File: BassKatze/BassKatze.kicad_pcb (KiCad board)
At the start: 2 copper layers, 55 x 54.9 mm, 50 parts, among them J1 Conn_01x02_Female, Q1 IRF7404, Q2 BSS138, SW1 SW_Push, U1 ATmega328-AU, U2 MSGEQ7, U3 TP4056

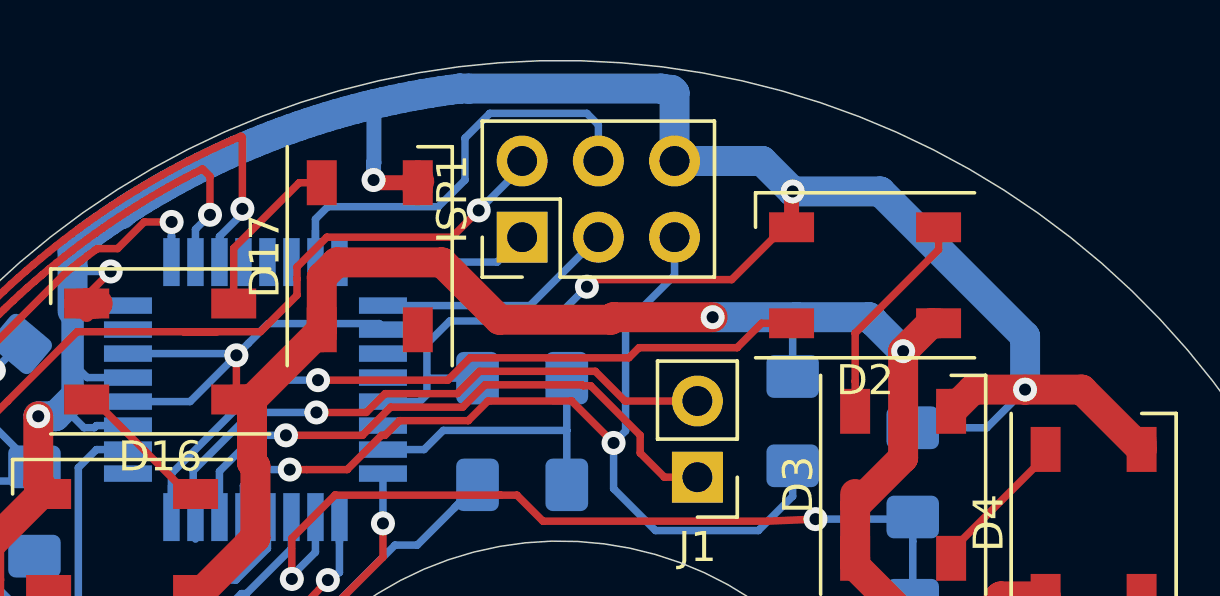
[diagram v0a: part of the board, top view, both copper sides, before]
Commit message: add pretective resistor to data pin of arduino
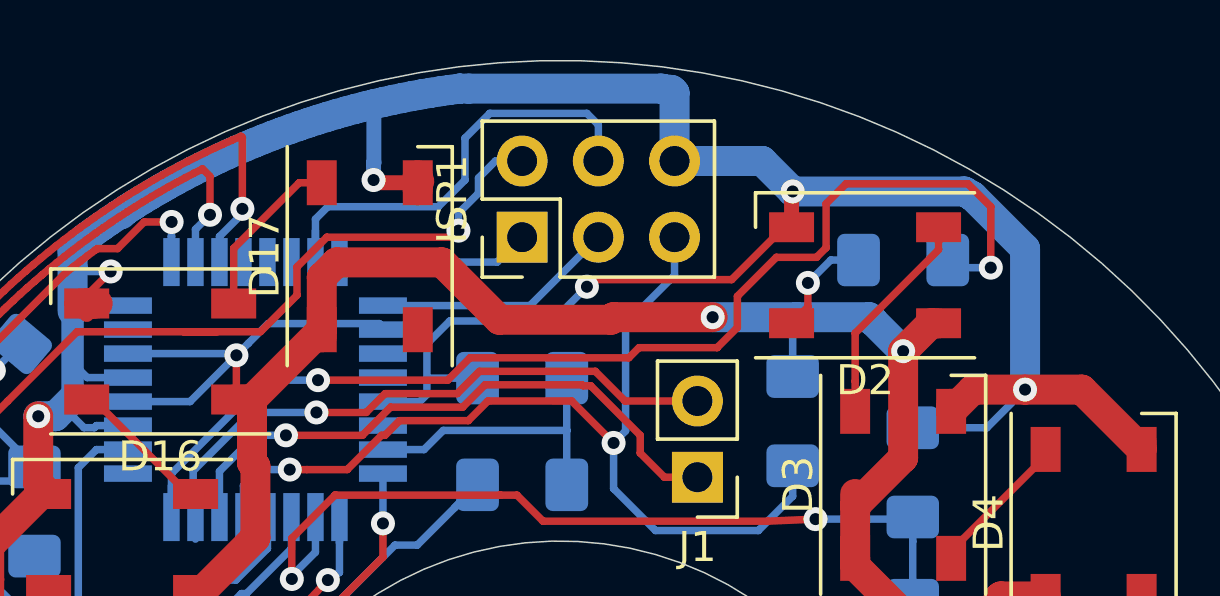
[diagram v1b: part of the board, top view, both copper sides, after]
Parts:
- added R14: 470Ohm, Resistor_SMD:R_1206_3216Metric_Pad1.42x1.75mm_HandSolder, B.Cu at (138.4, 106.2)
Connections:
- U1 pad 32: LED1 -> Net-(R14-Pad2)
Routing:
- net Net-(R14-Pad2): track 0.00 -> 39.2 mm, vias 0 -> 2
- net LED1: track 25.2 -> 3.57 mm
- net BAT-: track 283.6 -> 285.3 mm
- net 5V_Flash: track 27.5 -> 28.2 mm
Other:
- board text added: "BassKatze Rev 0.4"
- board text removed: "BassKatze Rev 0.3"

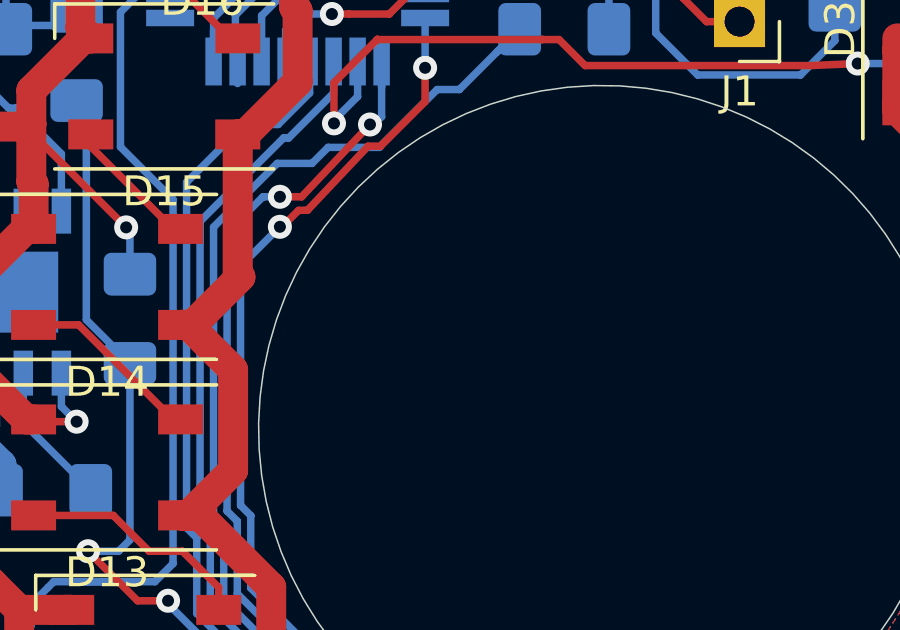
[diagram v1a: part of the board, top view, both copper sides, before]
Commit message: Added R16, added modes to sketch
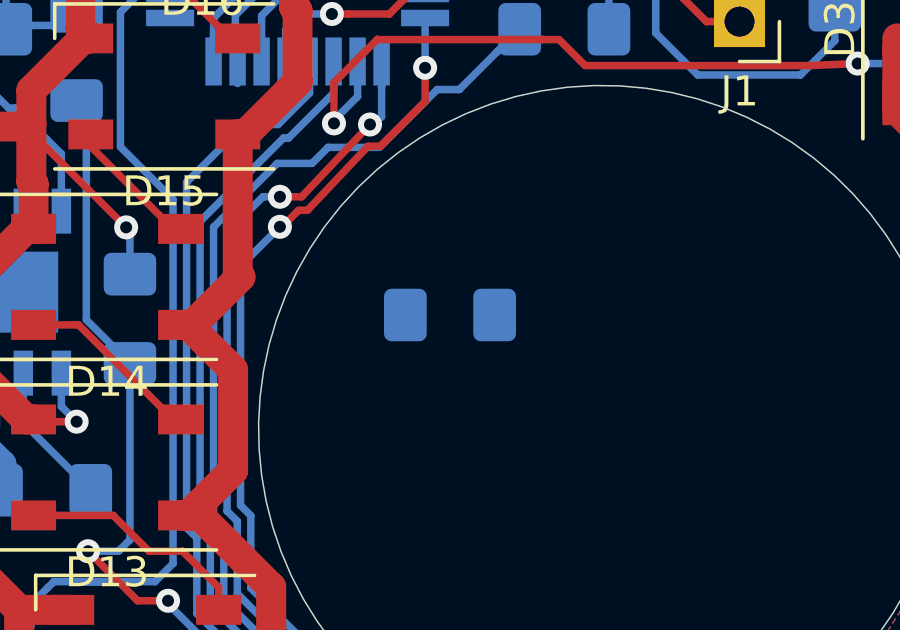
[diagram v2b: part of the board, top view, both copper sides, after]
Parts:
- added R15: 10k, Resistor_SMD:R_1206_3216Metric_Pad1.42x1.75mm_HandSolder, B.Cu at (121.9, 123.2)
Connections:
- D17 pad 4: (no net) -> Net-(D17-Pad4)
- U1 pad 1: (no net) -> Net-(U1-Pad1)
- U1 pad 12: (no net) -> Net-(U1-Pad12)
- U1 pad 13: (no net) -> Net-(U1-Pad13)
- U1 pad 14: (no net) -> Net-(U1-Pad14)
- U1 pad 19: (no net) -> Net-(U1-Pad19)
- U1 pad 20: (no net) -> Net-(U1-Pad20)
- U1 pad 22: (no net) -> Net-(U1-Pad22)
- U1 pad 7: (no net) -> Net-(U1-Pad7)
- U1 pad 8: (no net) -> Net-(U1-Pad8)
- U3 pad 9: (no net) -> Net-(U3-Pad9)
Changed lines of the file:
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@@
     (tracks 944)
     (zones 0)
-    (modules 51)
-    (nets 51)
+    (modules 52)
+    (nets 62)
   )
   (page A4)
@@
   (net 49 5V_Flash)
   (net 50 "Net-(R14-Pad2)")
+  (net 51 "Net-(D17-Pad4)")
+  (net 52 "Net-(U1-Pad22)")
+  (net 53 "Net-(U1-Pad20)")
+  (net 54 "Net-(U1-Pad19)")
+  (net 55 "Net-(U1-Pad14)")
+  (net 56 "Net-(U1-Pad13)")
+  (net 57 "Net-(U1-Pad12)")
+  (net 58 "Net-(U1-Pad8)")
+  (net 59 "Net-(U1-Pad7)")
+  (net 60 "Net-(U1-Pad1)")
+  (net 61 "Net-(U3-Pad9)")
   (net_class Default "This is the default net class."
     (clearance 0.2)
@@
     (add_net "Net-(D15-Pad4)")
     (add_net "Net-(D16-Pad4)")
+    (add_net "Net-(D17-Pad4)")
     (add_net "Net-(D18-Pad1)")
     (add_net "Net-(D2-Pad4)")
@@
     (add_net "Net-(R7-Pad1)")
     (add_net "Net-(RProg1-Pad1)")
+    (add_net "Net-(U1-Pad1)")
+    (add_net "Net-(U1-Pad12)")
+    (add_net "Net-(U1-Pad13)")
+    (add_net "Net-(U1-Pad14)")
+    (add_net "Net-(U1-Pad19)")
+    (add_net "Net-(U1-Pad20)")
+    (add_net "Net-(U1-Pad22)")
+    (add_net "Net-(U1-Pad7)")
+    (add_net "Net-(U1-Pad8)")
+    (add_net "Net-(U3-Pad9)")
     (add_net PWR)
     (add_net PWR_HOLD)
@@
   )
   (module Resistor_SMD:R_1206_3216Metric_Pad1.42x1.75mm_HandSolder (layer B.Cu)
+    (at 121.92 123.19)
+    (descr "Resistor SMD 1206 (3216 Metric), square (rectangular) end terminal, IPC_7351 nominal with elongated pad for handsoldering. (Body size source: http://www.tortai-tech.com/upload/download/2011102023233369053.pdf), generated with kicad-footprint-generator")
+    (tags "resistor handsolder")
+    (attr smd)
+    (fp_text reference R15 (at 0 1.82) (layer B.SilkS)
+      (effects (font (size 1 1) (thickness 0.15)) (justify mirror))
+    )
+    (fp_text value 10k (at 0 -1.82) (layer B.Fab)
+      (effects (font (size 1 1) (thickness 0.15)) (justify mirror))
+    )
+    (fp_text user %R (at 0 0) (layer B.Fab)
+      (effects (font (size 0.8 0.8) (thickness 0.12)) (justify mirror))
+    )
+    (fp_line (start 2.45 -1.12) (end -2.45 -1.12) (layer B.CrtYd) (width 0.05))
+    (fp_line (start 2.45 1.12) (end 2.45 -1.12) (layer B.CrtYd) (width 0.05))
+    (fp_line (start -2.45 1.12) (end 2.45 1.12) (layer B.CrtYd) (width 0.05))
+    (fp_line (start -2.45 -1.12) (end -2.45 1.12) (layer B.CrtYd) (width 0.05))
+    (fp_line (start -0.602064 -0.91) (end 0.602064 -0.91) (layer B.SilkS) (width 0.12))
+    (fp_line (start -0.602064 0.91) (end 0.602064 0.91) (layer B.SilkS) (width 0.12))
+    (fp_line (start 1.6 -0.8) (end -1.6 -0.8) (layer B.Fab) (width 0.1))
+    (fp_line (start 1.6 0.8) (end 1.6 -0.8) (layer B.Fab) (width 0.1))
+    (fp_line (start -1.6 0.8) (end 1.6 0.8) (layer B.Fab) (width 0.1))
+    (fp_line (start -1.6 -0.8) (end -1.6 0.8) (layer B.Fab) (width 0.1))
+    (pad 2 smd roundrect (at 1.4875 0) (size 1.425 1.75) (layers B.Cu B.Paste B.Mask) (roundrect_rratio 0.175439)
+      (net 18 Button))
+    (pad 1 smd roundrect (at -1.4875 0) (size 1.425 1.75) (layers B.Cu B.Paste B.Mask) (roundrect_rratio 0.175439)
+      (net 1 BAT-))
+    (model ${KISYS3DMOD}/Resistor_SMD.3dshapes/R_1206_3216Metric.wrl
+      (at (xyz 0 0 0))
+      (scale (xyz 1 1 1))
+      (rotate (xyz 0 0 0))
+    )
+  )
+  (module Resistor_SMD:R_1206_3216Metric_Pad1.42x1.75mm_HandSolder (layer B.Cu)
     (at 138.43 106.172)
     (descr "Resistor SMD 1206 (3216 Metric), square (rectangular) end terminal, IPC_7351 nominal with elongated pad for handsoldering. (Body size source: http://www.tortai-tech.com/upload/download/2011102023233369053.pdf), generated with kicad-footprint-generator")
@@
     (fp_line (start 1.95 2.45) (end 1.95 -2.45) (layer B.Fab) (width 0.15))
     (fp_line (start -0.95 2.45) (end 1.95 2.45) (layer B.Fab) (width 0.15))
-    (pad 9 smd rect (at 0 0 90) (size 2.7 3.6) (layers B.Cu B.Paste B.Mask))
+    (pad 9 smd rect (at 0 0 90) (size 2.7 3.6) (layers B.Cu B.Paste B.Mask)
+      (net 61 "Net-(U3-Pad9)"))
     (pad 8 smd rect (at 2.7 1.905 90) (size 1.5 0.65) (layers B.Cu B.Paste B.Mask)
       (net 2 "Net-(C1-Pad1)"))
@@
     (pad 3 smd rect (at -2.45 -1.6 90) (size 1.5 1) (layers F.Cu F.Paste F.Mask)
       (net 7 PWR))
-    (pad 4 smd rect (at -2.45 1.6 90) (size 1.5 1) (layers F.Cu F.Paste F.Mask))
+    (pad 4 smd rect (at -2.45 1.6 90) (size 1.5 1) (layers F.Cu F.Paste F.Mask)
+      (net 51 "Net-(D17-Pad4)"))
     (pad 2 smd rect (at 2.45 -1.6 90) (size 1.5 1) (layers F.Cu F.Paste F.Mask)
       (net 35 "Net-(D16-Pad4)"))
@@
     (pad 23 smd rect (at 4.25 2) (size 1.6 0.55) (layers B.Cu B.Paste B.Mask)
       (net 45 "Net-(R10-Pad2)"))
-    (pad 22 smd rect (at 4.25 1.2) (size 1.6 0.55) (layers B.Cu B.Paste B.Mask))
+    (pad 22 smd rect (at 4.25 1.2) (size 1.6 0.55) (layers B.Cu B.Paste B.Mask)
+      (net 52 "Net-(U1-Pad22)"))
     (pad 21 smd rect (at 4.25 0.4) (size 1.6 0.55) (layers B.Cu B.Paste B.Mask)
       (net 1 BAT-))
-    (pad 20 smd rect (at 4.25 -0.4) (size 1.6 0.55) (layers B.Cu B.Paste B.Mask))
-    (pad 19 smd rect (at 4.25 -1.2) (size 1.6 0.55) (layers B.Cu B.Paste B.Mask))
+    (pad 20 smd rect (at 4.25 -0.4) (size 1.6 0.55) (layers B.Cu B.Paste B.Mask)
+      (net 53 "Net-(U1-Pad20)"))
+    (pad 19 smd rect (at 4.25 -1.2) (size 1.6 0.55) (layers B.Cu B.Paste B.Mask)
+      (net 54 "Net-(U1-Pad19)"))
     (pad 18 smd rect (at 4.25 -2) (size 1.6 0.55) (layers B.Cu B.Paste B.Mask)
       (net 7 PWR))
@@
     (pad 15 smd rect (at 2 -4.25 270) (size 1.6 0.55) (layers B.Cu B.Paste B.Mask)
       (net 9 MOSI))
-    (pad 14 smd rect (at 1.2 -4.25 270) (size 1.6 0.55) (layers B.Cu B.Paste B.Mask))
-    (pad 13 smd rect (at 0.4 -4.25 270) (size 1.6 0.55) (layers B.Cu B.Paste B.Mask))
-    (pad 12 smd rect (at -0.4 -4.25 270) (size 1.6 0.55) (layers B.Cu B.Paste B.Mask))
+    (pad 14 smd rect (at 1.2 -4.25 270) (size 1.6 0.55) (layers B.Cu B.Paste B.Mask)
+      (net 55 "Net-(U1-Pad14)"))
+    (pad 13 smd rect (at 0.4 -4.25 270) (size 1.6 0.55) (layers B.Cu B.Paste B.Mask)
+      (net 56 "Net-(U1-Pad13)"))
+    (pad 12 smd rect (at -0.4 -4.25 270) (size 1.6 0.55) (layers B.Cu B.Paste B.Mask)
+      (net 57 "Net-(U1-Pad12)"))
     (pad 11 smd rect (at -1.2 -4.25 270) (size 1.6 0.55) (layers B.Cu B.Paste B.Mask)
       (net 36 STDBY))
@@
     (pad 9 smd rect (at -2.8 -4.25 270) (size 1.6 0.55) (layers B.Cu B.Paste B.Mask)
       (net 19 PWR_HOLD))
-    (pad 8 smd rect (at -4.25 -2.8) (size 1.6 0.55) (layers B.Cu B.Paste B.Mask))
-    (pad 7 smd rect (at -4.25 -2) (size 1.6 0.55) (layers B.Cu B.Paste B.Mask))
+    (pad 8 smd rect (at -4.25 -2.8) (size 1.6 0.55) (layers B.Cu B.Paste B.Mask)
+      (net 58 "Net-(U1-Pad8)"))
+    (pad 7 smd rect (at -4.25 -2) (size 1.6 0.55) (layers B.Cu B.Paste B.Mask)
+      (net 59 "Net-(U1-Pad7)"))
     (pad 6 smd rect (at -4.25 -1.2) (size 1.6 0.55) (layers B.Cu B.Paste B.Mask)
       (net 7 PWR))
@@
     (pad 2 smd rect (at -4.25 2) (size 1.6 0.55) (layers B.Cu B.Paste B.Mask)
       (net 18 Button))
-    (pad 1 smd rect (at -4.25 2.8) (size 1.6 0.55) (layers B.Cu B.Paste B.Mask))
+    (pad 1 smd rect (at -4.25 2.8) (size 1.6 0.55) (layers B.Cu B.Paste B.Mask)
+      (net 60 "Net-(U1-Pad1)"))
     (model ${KISYS3DMOD}/Package_QFP.3dshapes/TQFP-32_7x7mm_P0.8mm.wrl
       (at (xyz 0 0 0))
@@
   (segment (start 135.255 107.735) (end 134.71 108.28) (width 0.25) (layer F.Cu) (net 21))
   (segment (start 135.255 106.934) (end 135.255 107.735) (width 0.25) (layer F.Cu) (net 21))
-  (segment (start 114.04 114.74) (end 114.04 113.69) (width 0.25) (layer B.Cu) (net 50))
-  (via (at 118.925 110.175636) (size 0.8) (drill 0.4) (layers F.Cu B.Cu) (net 50))
-  (segment (start 118.925 110.175636) (end 117.154364 110.175636) (width 0.25) (layer B.Cu) (net 50))
-  (segment (start 114.04 113.29) (end 114.04 114.74) (width 0.25) (layer B.Cu) (net 50))
-  (segment (start 117.154364 110.175636) (end 114.04 113.29) (width 0.25) (layer B.Cu) (net 50))
   (segment (start 143.18 112.715) (end 143.18 112.485) (width 0.25) (layer F.Cu) (net 22))
   (segment (start 140.03 115.865) (end 143.18 112.715) (width 0.25) (layer F.Cu) (net 22))
@@
   (segment (start 123.606923 104.612077) (end 124.27501 103.94399) (width 0.25) (layer B.Cu) (net 49))
   (segment (start 123.606923 105.191923) (end 123.606923 104.612077) (width 0.25) (layer B.Cu) (net 49))
+  (segment (start 114.04 114.74) (end 114.04 113.69) (width 0.25) (layer B.Cu) (net 50))
+  (via (at 118.925 110.175636) (size 0.8) (drill 0.4) (layers F.Cu B.Cu) (net 50))
+  (segment (start 118.925 110.175636) (end 117.154364 110.175636) (width 0.25) (layer B.Cu) (net 50))
+  (segment (start 114.04 113.29) (end 114.04 114.74) (width 0.25) (layer B.Cu) (net 50))
+  (segment (start 117.154364 110.175636) (end 114.04 113.29) (width 0.25) (layer B.Cu) (net 50))
   (via (at 141.351 106.426) (size 0.8) (drill 0.4) (layers F.Cu B.Cu) (net 50))
   (segment (start 140.1715 106.426) (end 139.9175 106.172) (width 0.25) (layer B.Cu) (net 50))
